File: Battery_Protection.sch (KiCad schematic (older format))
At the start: 101 parts, among them J10 JST 2P-1.0, J11 JST 2P-1.0, J12 Conn_01x02_Female, J13 Conn_01x04_Male, J14 Conn_01x01_Female, J4 JST 2P-1.0, J5 JST 2P-1.0, J6 JST 2P-1.0, J7 JST 2P-1.0, J8 JST 2P-1.0, J9 JST 2P-1.0, Q2 2n7002K, Q4 AON7400A, Q6 AON7400A, Q7 2n7002K, SW1 SW_Push, SW2 SW_Push, U2 BQ294706DSGR, U3 ITV4030, U4 BQ40Z50

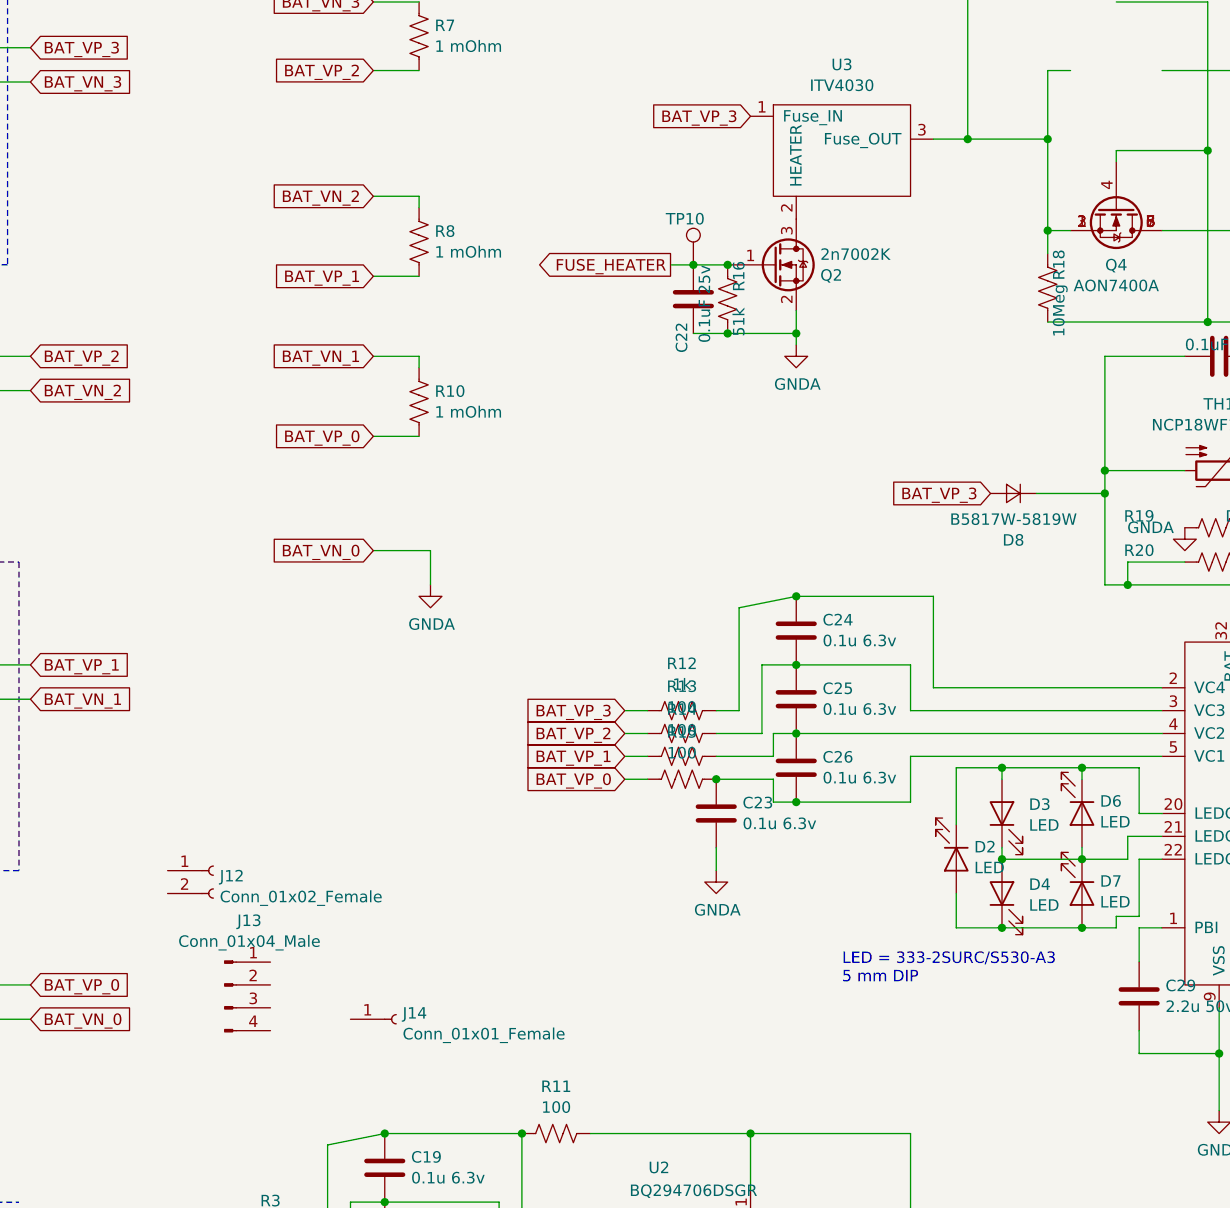
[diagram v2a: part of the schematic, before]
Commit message: Type_A_implemented. Sch "locked". PCB Layout started.
*Changelog:
*Type-a switching regulator (TBD -- need to check inductor,caps, stability. Maybe check both peripherial inductors?)
*Type-A load switch + connector + esd
*started layout..
*found out that my footprint for n fet is wrong. Fixing now, need to replace all of those.
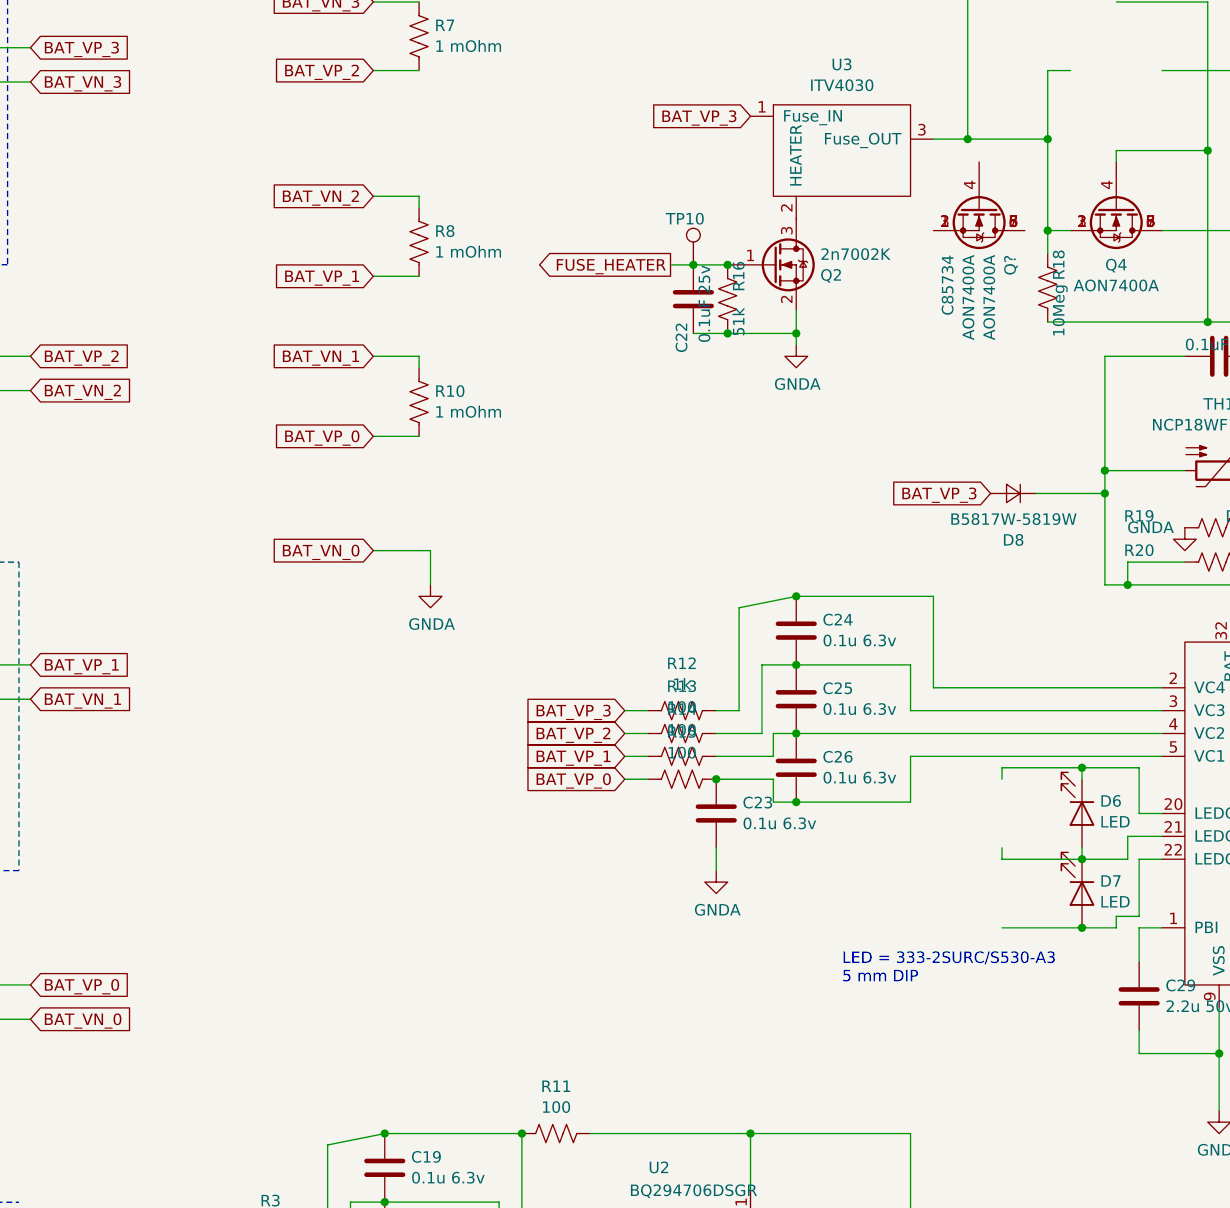
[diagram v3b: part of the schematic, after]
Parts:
- removed D2, D3, D4: LED, Diode_THT:D_DO-15_P3.81mm_Vertical_AnodeUp, symbol Device:LED
- removed J12: Conn_01x02_Female, symbol Connector:Conn_01x02_Female
- removed J13: Conn_01x04_Male, symbol Connector:Conn_01x04_Male
- removed J14: Conn_01x01_Female, symbol Connector:Conn_01x01_Female
- added Q?: AON7400A, lc_lib:SON-8_3.3X3.3MM, symbol SmartBattery:AON7400A
- SW1, SW2: footprint lc_lib:0402_R -> Button_Switch_SMD:SW_Push_1P1T_NO_6x6mm_H9.5mm; SKU B3F-1052 -> TS-1187A-C-G-B; lcsc (none) -> C318886
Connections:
- wire segments 303 -> 299
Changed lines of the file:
@@
 $Descr A4 11693 8268
 encoding utf-8
-Sheet 3 9
+Sheet 3 10
 Title ""
 Date ""
@@
 $EndComp
 $Comp
-L Device:LED D4
-U 1 1 5FFFF60F
-P 6300 4950
-F 0 "D4" V 6339 4833 50  0000 R CNN
-F 1 "LED" V 6248 4833 50  0000 R CNN
-F 2 "Diode_THT:D_DO-15_P3.81mm_Vertical_AnodeUp" H 6300 4950 50  0001 C CNN
-F 3 "~" H 6300 4950 50  0001 C CNN
-	1    6300 4950
-	0    -1   -1   0
-$EndComp
-$Comp
-L Device:LED D3
-U 1 1 5FFFF615
-P 6300 4600
-F 0 "D3" V 6339 4483 50  0000 R CNN
-F 1 "LED" V 6248 4483 50  0000 R CNN
-F 2 "Diode_THT:D_DO-15_P3.81mm_Vertical_AnodeUp" H 6300 4600 50  0001 C CNN
-F 3 "~" H 6300 4600 50  0001 C CNN
-	1    6300 4600
-	0    -1   -1   0
-$EndComp
-$Comp
 L Device:LED D6
 U 1 1 5FFFF61B
@@
 	0    1    1    0
 $EndComp
-$Comp
-L Device:LED D2
-U 1 1 5FFFF621
-P 6100 4800
-F 0 "D2" V 6047 4878 50  0000 L CNN
-F 1 "LED" V 6138 4878 50  0000 L CNN
-F 2 "Diode_THT:D_DO-15_P3.81mm_Vertical_AnodeUp" H 6100 4800 50  0001 C CNN
-F 3 "~" H 6100 4800 50  0001 C CNN
-	1    6100 4800
-	0    1    1    0
-$EndComp
-Wire Wire Line
-	6100 4950 6100 5100
-Wire Wire Line
-	6100 5100 6300 5100
 Wire Wire Line
 	6300 5100 6650 5100
-Connection ~ 6300 5100
 Wire Wire Line
 	6650 5100 6800 5100
@@
 Wire Wire Line
 	6300 4800 6300 4750
-Connection ~ 6300 4800
 Wire Wire Line
 	7000 4600 6900 4600
@@
 	6300 4400 6300 4450
 Connection ~ 6650 4400
-Wire Wire Line
-	6300 4400 6100 4400
-Wire Wire Line
-	6100 4400 6100 4650
-Connection ~ 6300 4400
 Text Notes 5600 5350 0    50   ~ 0
 LED = 333-2SURC/S530-A3\n5 mm DIP\n
@@
 F 0 "SW1" H 10150 5335 50  0000 C CNN
 F 1 "SW_Push" H 10150 5244 50  0000 C CNN
-F 2 "lc_lib:0402_R" H 10150 5250 50  0001 C CNN
+F 2 "Button_Switch_SMD:SW_Push_1P1T_NO_6x6mm_H9.5mm" H 10150 5250 50  0001 C CNN
 F 3 "~" H 10150 5250 50  0001 C CNN
-F 4 "B3F-1052" H 10150 5050 50  0001 C CNN "SKU"
+F 4 "TS-1187A-C-G-B" H 10150 5050 50  0001 C CNN "SKU"
+F 5 "C318886" H 10150 5050 50  0001 C CNN "lcsc"
 	1    10150 5050
-	1    0    0    -1
-$EndComp
-$Comp
-L Switch:SW_Push SW2
-U 1 1 6039D4EC
-P 10150 5400
-F 0 "SW2" H 10150 5685 50  0000 C CNN
-F 1 "SW_Push" H 10150 5594 50  0000 C CNN
-F 2 "lc_lib:0402_R" H 10150 5600 50  0001 C CNN
-F 3 "~" H 10150 5600 50  0001 C CNN
-F 4 "B3F-1052" H 10150 5400 50  0001 C CNN "SKU"
-	1    10150 5400
 	1    0    0    -1
 $EndComp
@@
 	1    8600 2150
 	0    -1   -1   0
-$EndComp
-$Comp
-L Connector:Conn_01x02_Female J12
-U 1 1 5FE89E75
-P 2850 4850
-F 0 "J12" H 2878 4826 50  0000 L CNN
-F 1 "Conn_01x02_Female" H 2878 4735 50  0000 L CNN
-F 2 "" H 2850 4850 50  0001 C CNN
-F 3 "~" H 2850 4850 50  0001 C CNN
-	1    2850 4850
-	1    0    0    -1
-$EndComp
-$Comp
-L Connector:Conn_01x04_Male J13
-U 1 1 5FE8B251
-P 2900 5350
-F 0 "J13" H 3008 5631 50  0000 C CNN
-F 1 "Conn_01x04_Male" H 3008 5540 50  0000 C CNN
-F 2 "" H 2900 5350 50  0001 C CNN
-F 3 "~" H 2900 5350 50  0001 C CNN
-	1    2900 5350
-	1    0    0    -1
-$EndComp
-$Comp
-L Connector:Conn_01x01_Female J14
-U 1 1 5FE8E98D
-P 3650 5500
-F 0 "J14" H 3678 5526 50  0000 L CNN
-F 1 "Conn_01x01_Female" H 3678 5435 50  0000 L CNN
-F 2 "" H 3650 5500 50  0001 C CNN
-F 3 "~" H 3650 5500 50  0001 C CNN
-	1    3650 5500
-	1    0    0    -1
 $EndComp
 $Comp
@@
 Wire Wire Line
 	6450 3200 6750 3200
+$Comp
+L Switch:SW_Push SW2
+U 1 1 60339F5D
+P 10150 5400
+F 0 "SW2" H 10150 5685 50  0000 C CNN
+F 1 "SW_Push" H 10150 5594 50  0000 C CNN
+F 2 "Button_Switch_SMD:SW_Push_1P1T_NO_6x6mm_H9.5mm" H 10150 5600 50  0001 C CNN
+F 3 "~" H 10150 5600 50  0001 C CNN
+F 4 "TS-1187A-C-G-B" H 10150 5400 50  0001 C CNN "SKU"
+F 5 "C318886" H 10150 5400 50  0001 C CNN "lcsc"
+	1    10150 5400
+	1    0    0    -1
+$EndComp
+$Comp
+L SmartBattery:AON7400A Q?
+U 1 1 604C6560
+P 6200 1950
+F 0 "Q?" H 6406 2087 50  0000 L CNN
+F 1 "AON7400A" H 6406 1996 50  0000 L CNN
+F 2 "lc_lib:SON-8_3.3X3.3MM" H 6850 2400 50  0001 C CNN
+F 3 "~" H 6200 1950 50  0001 C CNN
+F 4 "AON7400A" H 6406 1905 50  0000 L CNN "SKU"
+F 5 "C85734" H 6406 1814 50  0000 L CNN "LCSC"
+	1    6200 1950
+	0    1    1    0
+$EndComp
 $EndSCHEMATC

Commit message: Much layout. Wow
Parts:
- removed Q4, Q6: AON7400A, lc_lib:QFN-8_3X3X065P, symbol SmartBattery:AO4468
- added Q6: AON7400A, lc_lib:SON-8_3.3X3.3MM, symbol SmartBattery:AON7400A
- gave numbers to parts that had none: 1
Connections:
- wire segments 299 -> 303
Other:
- moved on the sheet: Q4
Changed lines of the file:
@@
 Connection ~ 3600 6000
 Wire Wire Line
-	5150 7000 5550 7000
+	5150 7000 5250 7000
 $Comp
 L Device:R_US R11
@@
 	1    950  2050
 	1    0    0    -1
-$EndComp
-$Comp
-L SmartBattery:AO4468 Q4
-U 1 1 60326882
-P 6800 1950
-F 0 "Q4" V 7051 1950 50  0000 C CNN
-F 1 "AON7400A " V 7142 1950 50  0000 C CNN
-F 2 "lc_lib:QFN-8_3X3X065P" H 7000 2050 50  0001 C CNN
-F 3 "~" H 6800 1950 50  0001 C CNN
-F 4 "C85734" V 6800 1950 50  0001 C CNN "LCSC"
-	1    6800 1950
-	0    1    1    0
-$EndComp
-$Comp
-L SmartBattery:AO4468 Q6
-U 1 1 60353110
-P 8600 2150
-F 0 "Q6" V 8943 2150 50  0000 C CNN
-F 1 "AON7400A " V 8852 2150 50  0000 C CNN
-F 2 "lc_lib:QFN-8_3X3X065P" H 8800 2250 50  0001 C CNN
-F 3 "~" H 8600 2150 50  0001 C CNN
-F 4 "AON7400A " V 8600 2150 50  0001 C CNN "SKU"
-	1    8600 2150
-	0    -1   -1   0
 $EndComp
 $Comp
@@
 $EndComp
 $Comp
-L SmartBattery:AON7400A Q?
+L SmartBattery:AON7400A Q4
 U 1 1 604C6560
-P 6200 1950
-F 0 "Q?" H 6406 2087 50  0000 L CNN
-F 1 "AON7400A" H 6406 1996 50  0000 L CNN
-F 2 "lc_lib:SON-8_3.3X3.3MM" H 6850 2400 50  0001 C CNN
-F 3 "~" H 6200 1950 50  0001 C CNN
-F 4 "AON7400A" H 6406 1905 50  0000 L CNN "SKU"
-F 5 "C85734" H 6406 1814 50  0000 L CNN "LCSC"
-	1    6200 1950
+P 6800 1950
+F 0 "Q4" H 7050 2000 50  0000 L CNN
+F 1 "AON7400A" H 7050 1900 50  0000 L CNN
+F 2 "lc_lib:SON-8_3.3X3.3MM" H 7450 2400 50  0001 C CNN
+F 3 "~" H 6800 1950 50  0001 C CNN
+F 4 "AON7400A" H 7006 1905 50  0001 L CNN "SKU"
+F 5 "C85734" H 7006 1814 50  0001 L CNN "LCSC"
+	1    6800 1950
 	0    1    1    0
 $EndComp
+$Comp
+L SmartBattery:AON7400A Q6
+U 1 1 600179EF
+P 8600 2150
+F 0 "Q6" V 8950 2200 50  0000 L CNN
+F 1 "AON7400A" V 8850 2100 50  0000 L CNN
+F 2 "lc_lib:SON-8_3.3X3.3MM" H 9250 2600 50  0001 C CNN
+F 3 "~" H 8600 2150 50  0001 C CNN
+F 4 "AON7400A" H 8806 2105 50  0001 L CNN "SKU"
+F 5 "C85734" H 8806 2014 50  0001 L CNN "LCSC"
+	1    8600 2150
+	0    -1   -1   0
+$EndComp
+Wire Wire Line
+	8350 5500 8250 5500
+Wire Wire Line
+	8250 5500 8250 5450
+Connection ~ 8350 5500
+Wire Wire Line
+	5250 6850 5250 7000
+Connection ~ 5250 7000
+Wire Wire Line
+	5250 7000 5550 7000
 $EndSCHEMATC
